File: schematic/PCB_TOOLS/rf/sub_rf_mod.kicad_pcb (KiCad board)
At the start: 2 copper layers, 69.1 x 50 mm, 39 parts, among them J4B1 Conn_01x08

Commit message: updated gerbers and main/rf exports
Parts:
- moved RF_R8 15.3 mm to (155.2, 92.1)
- moved RF_R11 15.2 mm to (132.8, 87.0)
- moved RF_R12 15.2 mm to (142.2, 90.0)
- moved RF_R7 15.2 mm to (159.3, 92.1)
- moved RF_C2 15.2 mm to (126.5, 88.8)
- moved RF_JP1 15.2 mm to (122.7, 81.2)
- moved RF_C10 15.2 mm to (169.4, 102.7)
- moved RF_C12 15.2 mm to (152.6, 106.8)
- moved RF_C3 15.2 mm to (130.3, 102.3)
- moved RF_D1 15.2 mm to (122.4, 109.1)
- moved RF_L2 15.2 mm to (160.3, 98.9)
- moved RF_R10 15.2 mm to (140.5, 83.9)
- moved RF_R2 15.2 mm to (126.7, 98.9)
- moved RF_R4 15.2 mm to (137.9, 114.2)
- moved RF_SW1 15.2 mm to (136.3, 80.0)
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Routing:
- net (no net): track 612.3 -> 613.2 mm

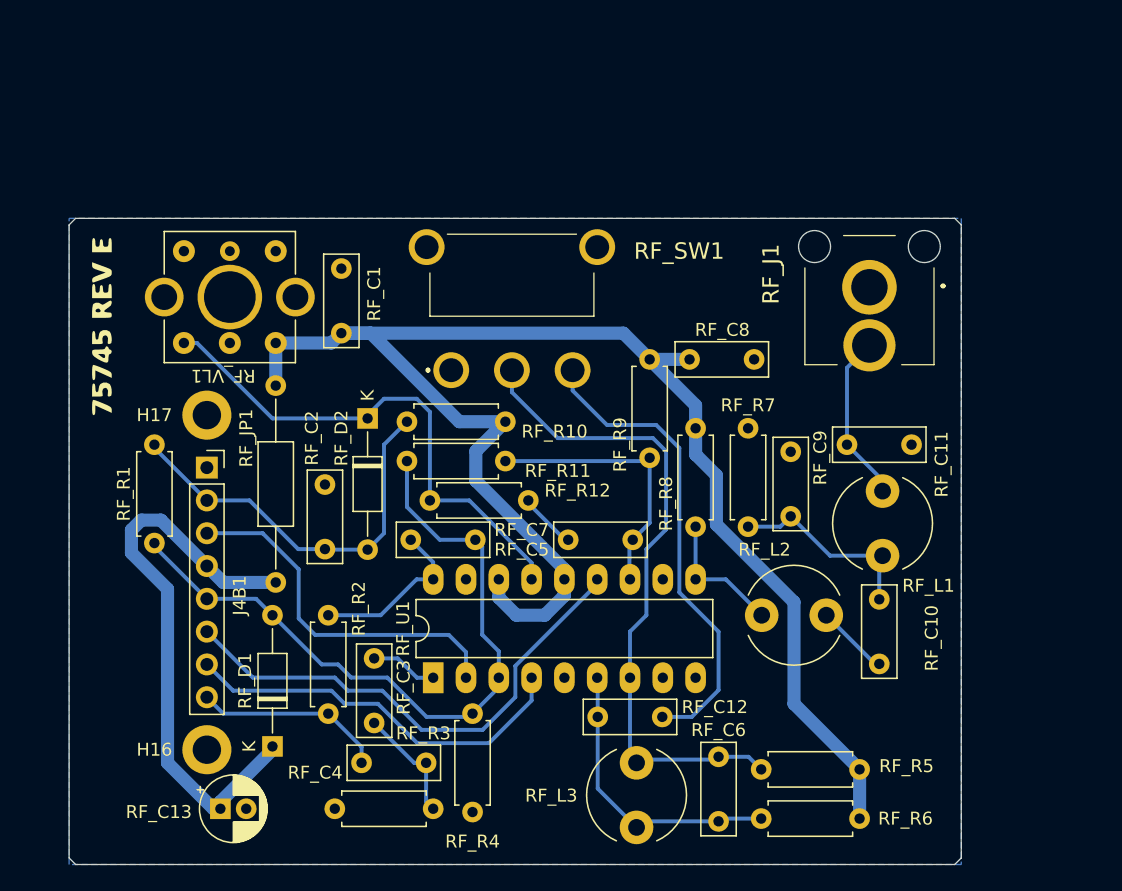
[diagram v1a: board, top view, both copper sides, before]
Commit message: fixed the switch for the sub-rf board to match the original coleco for chan 3/4 selection
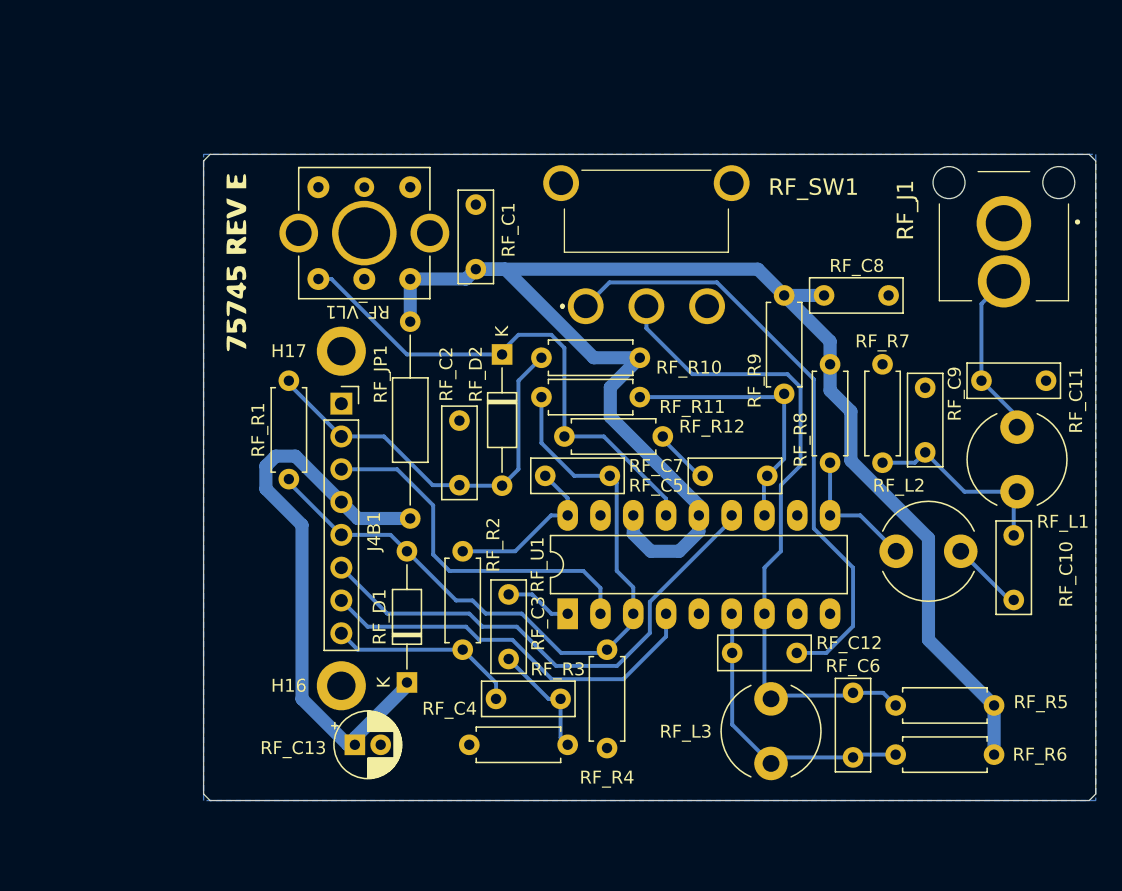
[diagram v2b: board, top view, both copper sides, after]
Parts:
- moved RF_C3 11.5 mm to (140.7, 97.3)
- moved RF_C4 11.5 mm to (144.7, 105.4)
- moved RF_D1 11.5 mm to (132.8, 104.1)
- moved RF_L1 11.5 mm to (180.1, 89.4)
- moved RF_L2 11.5 mm to (170.7, 94.0)
- moved RF_R10 11.5 mm to (150.9, 79.0)
- moved RF_R4 11.5 mm to (148.3, 109.2)
- moved RF_R8 11.5 mm to (165.6, 87.1)
- moved RF_SW1 11.5 mm to (146.7, 75.0)
- moved RF_U1 11.5 mm to (145.3, 98.8)
- moved RF_C5 11.5 mm to (143.6, 88.1)
- moved J4B1 11.5 mm to (127.8, 82.5)
- moved RF_C2 11.5 mm to (136.9, 83.9)
- moved RF_JP1 11.5 mm to (133.1, 76.2)
- moved RF_R2 11.5 mm to (137.2, 94.0)
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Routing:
- net (no net): track 613.2 -> 623.4 mm
